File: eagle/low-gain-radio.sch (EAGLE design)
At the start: 109 parts, among them Y1 32MHz

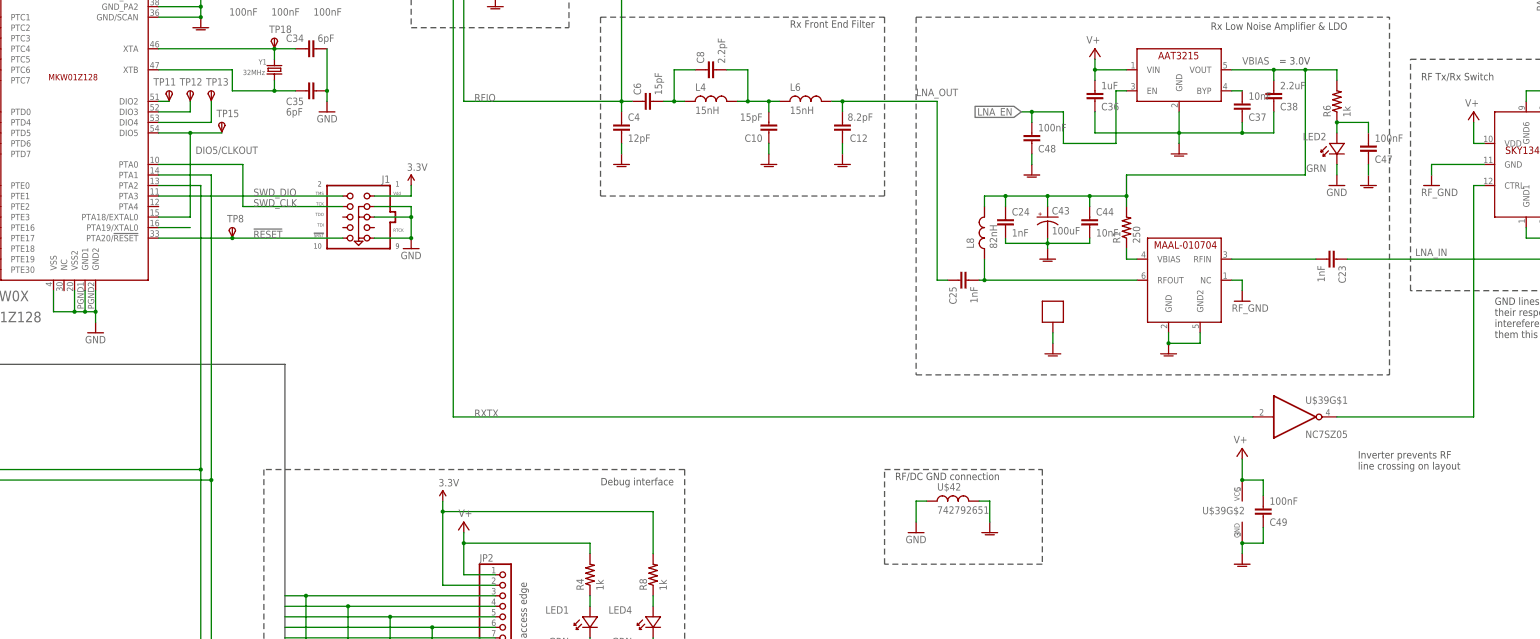
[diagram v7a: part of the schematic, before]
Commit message: Poor, poor Jake. We just axe murdeded his board. Figured out RF and digital ground, and decided to route power through the RF ground entry point. Added TOVA test point, which is better than current one (smaller, better symbol).
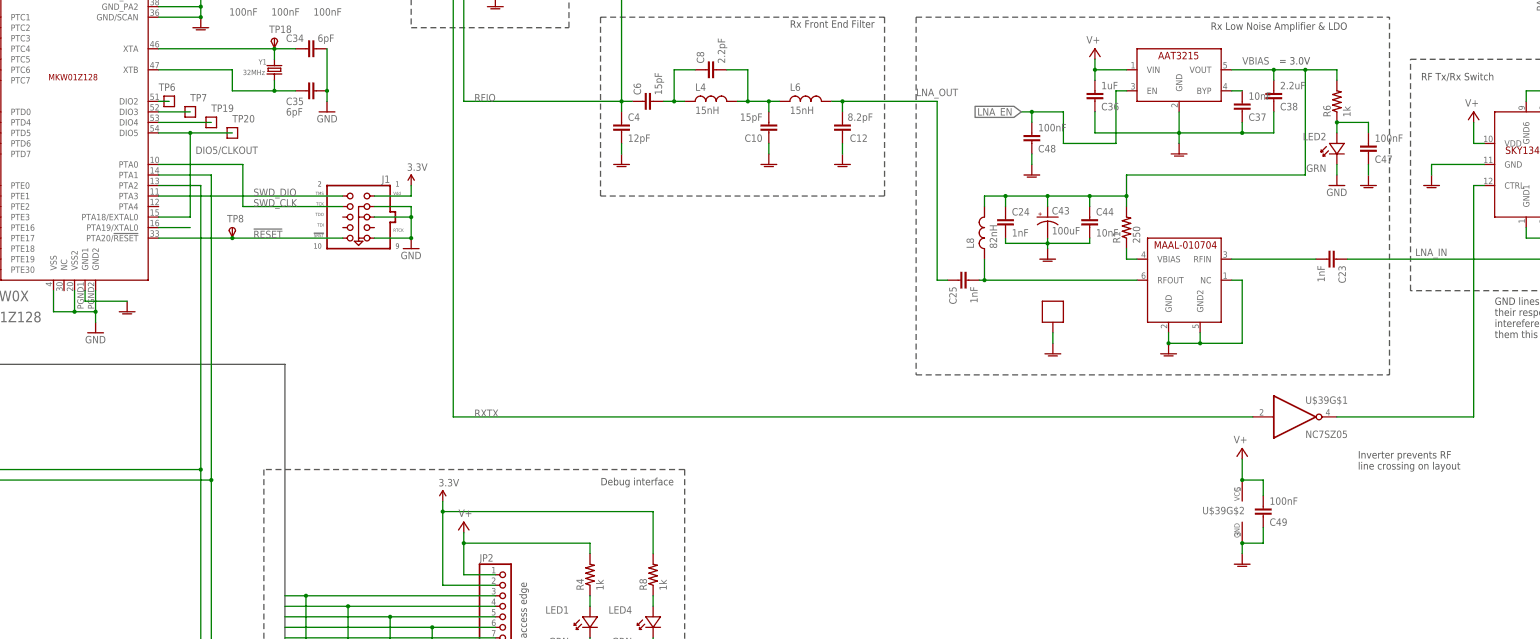
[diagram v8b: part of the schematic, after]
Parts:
- removed TP11, TP12, TP13, TP15: TPSPAD1-13, testpad:TPSPAD1-13
- removed U$42: 742792651, psas_c3_team05:742792651
- added TP19, TP20, TP6, TP7: TEST-POINT, Tova:TEST-POINT
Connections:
- removed net RF_GND: C1.1, C10.1, C11.1, C12.1, C13.1, C15.1, C16.1, C17.1, C18.1, C19.1, C2.2, C20.1, C21.1, C22.1, C24.2, C3.2, C30.1, C31.1, C32.1, C33.1, C36.1, C37.1, C38.1, C4.2, C43.-, C44.2, C45.1, C46.1, C47.1, C48.1, C49.1, C9.1, CF2.SHIELD, KW0X.GND/SCAN, KW0X.GND_PA1, KW0X.GND_PA2, LNA.GND, LNA.GND2, PA.GND, PA.GND1, PA.GND2, PA.GND3, PA.GND4, PA.GND5, SH1.P$1, SH2.P$1, TRSWITCH.GND1, TRSWITCH.GND2, TRSWITCH.GND3, TRSWITCH.GND4, TRSWITCH.GND5, TRSWITCH.GND6, U$39G$2.GND, U$42.2, U$7.GND, U$9.GND
- new net RIP: C1.1, C10.1, C11.1, C12.1, C13.1, C15.1, C16.1, C17.1, C18.1, C19.1, C2.2, C20.1, C21.1, C22.1, C24.2, C3.2, C30.1, C31.1, C32.1, C33.1, C36.1, C37.1, C38.1, C4.2, C43.-, C44.2, C45.1, C46.1, C47.1, C48.1, C49.1, C9.1, CF2.SHIELD, KW0X.GND/SCAN, KW0X.GND1, KW0X.GND_PA1, KW0X.GND_PA2, LNA.GND, LNA.GND2, LNA.NC, PA.GND, PA.GND1, PA.GND2, PA.GND3, PA.GND4, PA.GND5, SH1.P$1, SH2.P$1, TRSWITCH.GND, TRSWITCH.GND1, TRSWITCH.GND2, TRSWITCH.GND3, TRSWITCH.GND4, TRSWITCH.GND5, TRSWITCH.GND6, U$39G$2.GND, U$7.GND, U$9.GND
- net DIO2: now also TP6.1; no longer TP11.PP
- net DIO3: now also TP7.1; no longer TP12.PP
- net DIO4: now also TP19.1; no longer TP13.PP
- net DIO5/CLKOUT: now also TP20.1; no longer TP15.PP
- net GND: no longer KW0X.GND1, LNA.NC, TRSWITCH.GND, U$42.1
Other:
- note removed: "RF/DC GND connection"
